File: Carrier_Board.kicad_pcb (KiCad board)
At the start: 4 copper layers, 190 x 110 mm, 269 parts, among them J10 Conn_01x03_Pin, J11 Conn_01x03_Pin, J12 Conn_01x04_Pin, J13 Conn_01x04_Pin, J14 Conn_01x03_Pin, J15 Bus_M.2_Socket_M, J16 Bus_M.2_Socket_E, J17 Barrel_Jack_Switch, J18 USB_C_Receptacle_USB2.0_16P, J19 Conn_01x04_Pin, J2 Bus_PCI_Express_x4, J20 Conn_01x04_Pin, J21 Conn_01x04_Pin, J3 HDMI_A, J4 USB3_A_Stacked, J5 USB_A_Stacked, J6 RJ45_RB1-125B8G1A, J7 Conn_01x04_Pin, J78 Conn_01x03_Pin, J8 Conn_01x03_Pin, J9 Conn_01x04_Pin, M1 Fan_4pin, M2 Fan_4pin, Q1 2N7002, Q2 2SK3018, Q3 2SK3018, Q5 2N7002, Q6 2N7002, Q7 AON7262E, Q8 2N7002, Q85 2SK3018, SW1 SW_Push, SW2 SW_Push, U1 D3V3XA4B10LP, U10 D3V3XA4B10LP, U11 D3V3XA4B10LP, U12 D3V3XA4B10LP, U13 TL431DBZ, U14 CH224K, U15 LM2734X, U16 LM2734X, U17 D3V3XA4B10LP, U2 D3V3XA4B10LP, U3 D3V3XA4B10LP, U4 D3V3XA4B10LP, U5 D3V3XA4B10LP, U6 RTL8111H-CG-RH, U7 D3V3XA4B10LP, U8 D3V3XA4B10LP, U9 D3V3XA4B10LP, Y1 25MHz

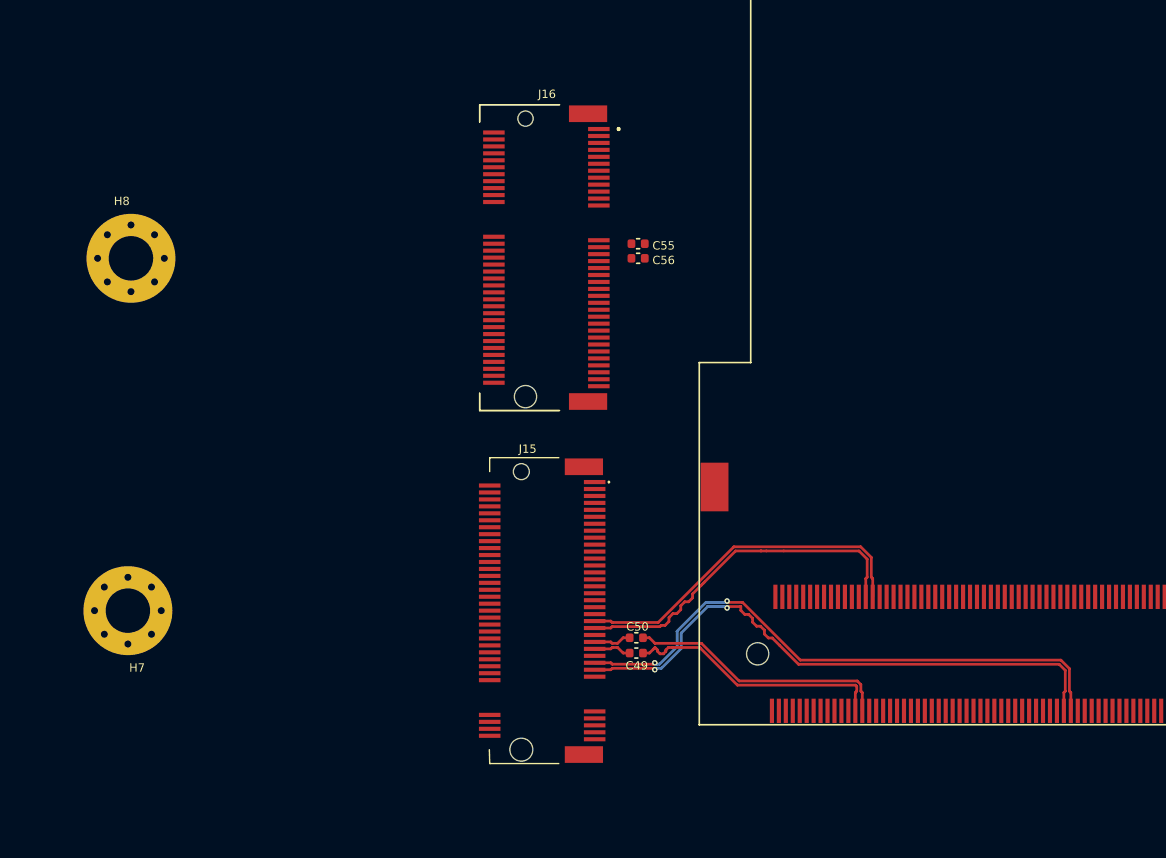
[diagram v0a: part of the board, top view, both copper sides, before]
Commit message: finished the differentail pair routing for the m.2 keys
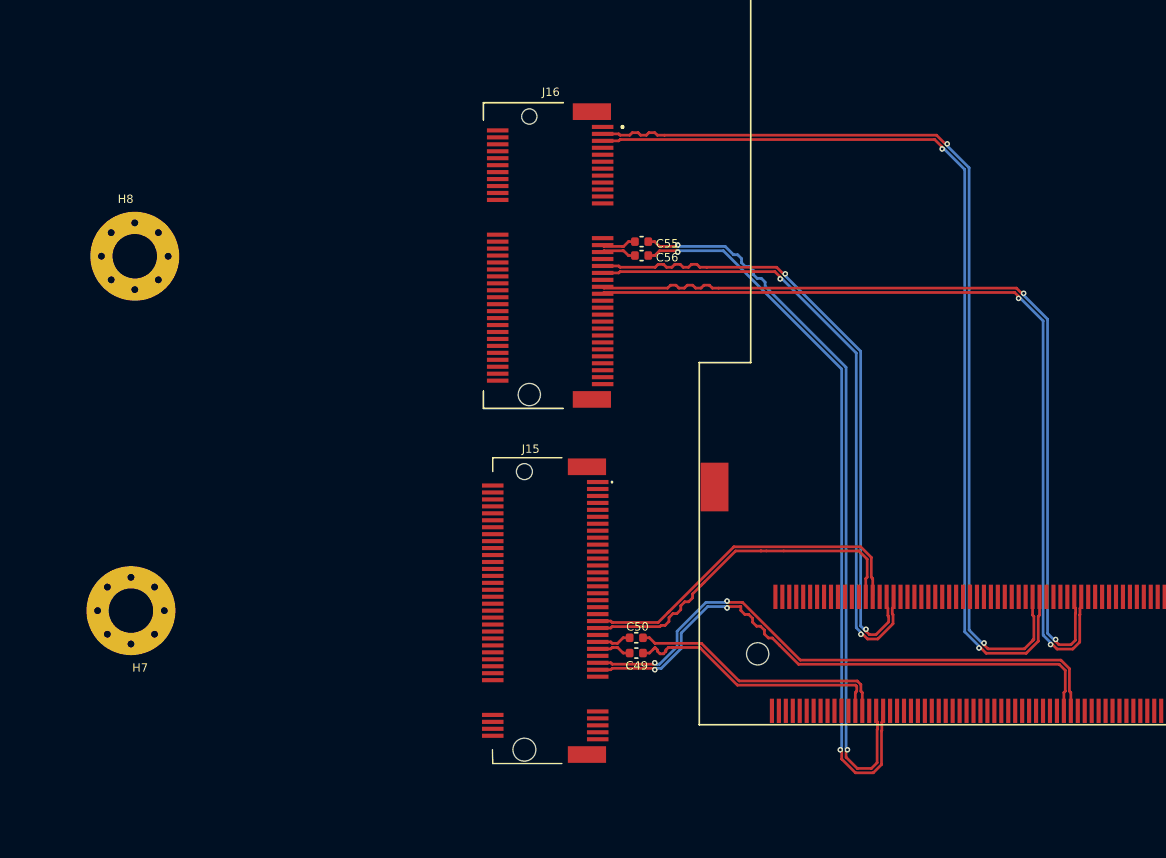
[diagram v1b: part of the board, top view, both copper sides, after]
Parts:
- moved C56 0.32 mm to (92.5, 82.0)
- moved H8 0.31 mm to (56.1, 82.0)
- moved J16 0.31 mm to (89.8, 72.7)
- moved C55 0.29 mm to (92.5, 81.0)
- moved H7 0.22 mm to (55.8, 107.5)
- moved J15 0.22 mm to (85.8, 107.5)
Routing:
- net /LattePanda Module/USB_2_P7+: track 0.00 -> 69.9 mm, vias 0 -> 2
- net /LattePanda Module/USB_2_P7-: track 0.00 -> 69.9 mm, vias 0 -> 2
- net /LattePanda Module/REFCLK3+: track 0.00 -> 61.9 mm, vias 0 -> 2
- net /LattePanda Module/REFCLK3-: track 0.00 -> 61.9 mm, vias 0 -> 2
- net /LattePanda Module/HSIO_3_TX+: track 0.00 -> 53.2 mm, vias 0 -> 2
- net /LattePanda Module/HSIO_3_TX-: track 0.00 -> 53.2 mm, vias 0 -> 2
- net /LattePanda Module/HSIO_3_RX+: track 0.00 -> 46.1 mm, vias 0 -> 2
- net /LattePanda Module/HSIO_3_RX-: track 0.00 -> 46.1 mm, vias 0 -> 2
- net /M.2 M Key/CON_PCIE_TX0+: track 0.00 -> 2.50 mm
- net /M.2 M Key/CON_PCIE_TX0-: track 0.00 -> 2.50 mm

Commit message: Created new Heiarchal sheet for audio, and started to arrange passive components for the HDMI connector
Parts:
- removed Q85: 2SK3018, A_HDJ_Library:SOT-23
- removed R143: 2.2K/1%, A_HDJ_Library:R_0402_1005Metric
- added Q4: 2SK3018, A_HDJ_Library:SOT-23, F.Cu at (152.3, 130.4)
- added R19: 2.2K/1%, A_HDJ_Library:R_0402_1005Metric, F.Cu at (149.4, 129.5)
- moved F2 321.5 mm to (86.6, 135.3)
- moved F3 321.5 mm to (86.6, 138.2)
- moved C30 308.3 mm to (86.6, 132.6)
- moved F4 305.1 mm to (103.3, 138.3)
- moved C31 293.1 mm to (103.3, 135.6)
- moved C26 287.2 mm to (107.6, 136.1)
- moved C27 287.2 mm to (107.6, 138.1)
- moved C32 285.1 mm to (111.2, 136.3)
- moved C28 284.1 mm to (107.8, 132.3)
- moved C29 284.1 mm to (107.8, 134.3)
- moved TP2 275.7 mm to (52.6, 122.1)
- moved Q1 272.2 mm to (131.0, 153.6)
- moved Q2 271.8 mm to (124.4, 142.7)
- moved Q3 271.8 mm to (124.4, 147.2)
- moved C17 259.9 mm to (131.8, 139.5)
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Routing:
- net Net-(J15-DEVSLP): track 0.00 -> 37.2 mm
- net Net-(D9-K): track 0.00 -> 13.9 mm
- net Net-(J16-SUSCLK): track 0.00 -> 3.63 mm
- net Net-(J16-~{W_DISABLE2}): track 0.00 -> 2.93 mm
- net Net-(J16-~{W_DISABLE1}): track 0.00 -> 2.64 mm
- net Net-(J15-SUSCLK): track 0.00 -> 2.53 mm
- net /M.2 M Key/CLKREQM: track 0.00 -> 2.53 mm
- net /M.2 M Key/CLKREQE: track 0.00 -> 2.29 mm
- net +3.3V: track 0.00 -> 1.20 mm

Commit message: HDM placement and some routing complete
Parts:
- moved C17 18.3 mm to (149.7, 136.0), turned to -90 degrees
- moved C18 17.8 mm to (148.7, 136.0), turned to -90 degrees
- moved C19 16.8 mm to (146.8, 135.9), turned to -90 degrees
- moved R19 15.7 mm to (160.2, 140.8)
- moved C20 11.7 mm to (145.8, 135.9), turned to -90 degrees
- moved C22 11.3 mm to (143.1, 135.9), turned to -90 degrees
- moved C21 10.9 mm to (144.1, 135.9), turned to -90 degrees
- moved Q4 10.6 mm to (157.2, 139.8), turned to 180 degrees
- moved U2 9.39 mm to (144.4, 143.5), turned to -90 degrees
- moved R7 9.13 mm to (139.5, 138.6)
- moved C24 6.02 mm to (140.0, 136.0), turned to -90 degrees
- moved C23 4.96 mm to (141.0, 136.0), turned to -90 degrees
- moved R10 3.89 mm to (144.3, 138.6)
- moved R9 3.76 mm to (142.7, 138.6)
- moved J6 3.60 mm to (164.4, 138.5)
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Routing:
- net /HDMI/DDI_B_TX3+: track 0.00 -> 26.6 mm
- net /HDMI/DDI_B_TX3-: track 0.00 -> 26.6 mm
- net /HDMI/DDI_B_TX2+: track 0.00 -> 26.0 mm
- net /HDMI/DDI_B_TX2-: track 0.00 -> 26.0 mm
- net /HDMI/DDI_B_TX1+: track 0.00 -> 25.5 mm
- net /HDMI/DDI_B_TX1-: track 0.00 -> 25.5 mm
- net /HDMI/DDI_B_TX0+: track 0.00 -> 25.0 mm
- net /HDMI/DDI_B_TX0-: track 0.00 -> 25.0 mm
- net /HDMI/TMDS_CK-: track 0.00 -> 14.3 mm
- net /HDMI/TMDS_CK+: track 0.00 -> 14.3 mm
- net /HDMI/TMDS_D0+: track 0.00 -> 12.7 mm
- net /HDMI/TMDS_D0-: track 0.00 -> 12.6 mm
- net /HDMI/TMDS_D2+: track 0.00 -> 12.3 mm
- net /HDMI/TMDS_D2-: track 0.00 -> 12.3 mm
- net /HDMI/TMDS_D1-: track 0.00 -> 12.1 mm
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
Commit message: HMI coponents placed and routed compete
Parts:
- removed R132, R134: 2.2k/1%, A_HDJ_Library:R_0402_1005Metric
- added R15: 2.2k/1%, A_HDJ_Library:R_0402_1005Metric, F.Cu at (135.5, 141.9)
- added R18: 2.2k/1%, A_HDJ_Library:R_0402_1005Metric, F.Cu at (133.9, 141.9)
- moved F1 274.5 mm to (131.8, 153.2)
- moved D4 273.3 mm to (131.3, 146.3), turned to -90 degrees
- moved C25 268.9 mm to (131.2, 151.8)
- moved D3 243.5 mm to (132.3, 141.9), turned to 90 degrees
- moved D1 240.5 mm to (137.1, 141.9), turned to 90 degrees
- moved C53 238.2 mm to (78.0, 97.3)
- moved C54 238.0 mm to (78.0, 98.3)
- moved C51 233.8 mm to (78.0, 95.3)
- moved C52 233.5 mm to (78.0, 96.3)
- moved C32 23.0 mm to (88.2, 136.3)
- moved C26 23.0 mm to (84.6, 136.1)
- moved C27 23.0 mm to (84.6, 138.1)
- moved C28 23.0 mm to (84.7, 132.3)
- moved C29 23.0 mm to (84.7, 134.3)
- moved C31 23.0 mm to (80.3, 135.6)
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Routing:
- net /HDMI/DDI_B_HPD: track 0.00 -> 38.8 mm, vias 0 -> 2
- net /HDMI/DDI_DDC_SCA: track 0.00 -> 28.6 mm
- net /HDMI/DDI_DDC_SCL: track 0.00 -> 28.2 mm
- net Net-(Q4-D): track 0.00 -> 19.8 mm, vias 0 -> 9
- net /HDMI/DDC_SCA: track 0.00 -> 16.5 mm
- net 5V_HDMI_VCC: track 0.00 -> 16.0 mm, vias 0 -> 2
- net /HDMI/HPD: track 0.00 -> 14.8 mm
- net /HDMI/DDC_SCL: track 0.00 -> 13.8 mm
- net Net-(J3-+5V): track 0.00 -> 12.4 mm
- net Net-(Q1-S): track 0.00 -> 4.52 mm
- net Net-(Q4-G): track 0.00 -> 2.07 mm

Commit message: positioning components for ehternet and USB connections and routing
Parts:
- moved U6 264.7 mm to (98.5, 128.2)
- moved U7 260.7 mm to (89.7, 128.5)
- moved U8 260.7 mm to (92.7, 128.5)
- moved BT78 169.2 mm to (220.7, 129.3)
- moved J10 168.9 mm to (205.1, 53.0)
- moved J11 168.9 mm to (191.7, 53.0)
- moved J14 168.9 mm to (196.4, 53.1)
- moved J8 168.9 mm to (200.8, 53.1)
- moved C46 77.9 mm to (94.3, 132.8)
- moved R24 77.9 mm to (90.0, 132.3)
- moved R25 77.9 mm to (90.0, 134.3)
- moved J6 77.9 mm to (86.5, 138.6)
- moved C26 15.8 mm to (68.9, 136.1)
- moved C27 15.8 mm to (68.9, 138.1)
- moved C28 15.8 mm to (69.0, 132.3)
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
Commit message: A little more adjusting before routing
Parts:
- moved U3 332.2 mm to (50.1, 144.3)
- moved F5 287.1 mm to (120.7, 135.9)
- moved U5 283.6 mm to (106.0, 137.8)
- moved U14 160.7 mm to (214.8, 83.2)
- moved Q7 149.2 mm to (198.3, 103.6)
- moved C31 54.1 mm to (118.5, 132.6)
- moved C28 48.9 mm to (117.8, 136.1)
- moved C29 48.9 mm to (117.8, 138.0)
- moved C26 6.25 mm to (63.9, 132.2)
- moved C27 6.25 mm to (63.9, 134.2)
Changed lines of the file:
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@@
 	(footprint "A_HDJ_Library:C_0603_1608Metric"
 		(layer "F.Cu")
-		(at 64.529999 135.59)
+		(at 118.5 132.55)
 		(descr "Capacitor SMD 0603 (1608 Metric), square (rectangular) end terminal, IPC_7351 nominal, (Body size source: IPC-SM-782 page 76, https://www.pcb-3d.com/wordpress/wp-content/uploads/ipc-sm-782a_amendment_1_and_2.pdf), generated with kicad-footprint-generator")
 		(tags "capacitor")
@@
 	(footprint "A_HDJ_Library:C_0402_1005Metric"
 		(layer "F.Cu")
-		(at 68.859999 136.09)
+		(at 63.93 132.25)
 		(descr "Capacitor SMD 0402 (1005 Metric), square (rectangular) end terminal, IPC_7351 nominal, (Body size source: IPC-SM-782 page 76, https://www.pcb-3d.com/wordpress/wp-content/uploads/ipc-sm-782a_amendment_1_and_2.pdf), generated with kicad-footprint-generator")
 		(tags "capacitor")
@@
 	(footprint "A_HDJ_Library:Fuse_0805_2012Metric"
 		(layer "F.Cu")
-		(at 379.325 11.15)
+		(at 120.7375 135.9)
 		(descr "Fuse SMD 0805 (2012 Metric), square (rectangular) end terminal, IPC_7351 nominal, (Body size source: https://docs.google.com/spreadsheets/d/1BsfQQcO9C6DZCsRaXUlFlo91Tg2WpOkGARC1WS5S8t0/edit?usp=sharing), generated with kicad-footprint-generator")
 		(tags "fuse")
@@
 	(footprint "A_HDJ_Library:MOSFET_PDFN8_3.3x3.3"
 		(layer "F.Cu")
-		(at 296.425 -8.825)
+		(at 198.3 103.56)
 		(descr " DFN 3x3  EP")
 		(tags "MOSFET (N-Channel)")
@@
 	(footprint "A_HDJ_Library:C_0402_1005Metric"
 		(layer "F.Cu")
-		(at 68.979999 132.34)
+		(at 117.775 136.05)
 		(descr "Capacitor SMD 0402 (1005 Metric), square (rectangular) end terminal, IPC_7351 nominal, (Body size source: IPC-SM-782 page 76, https://www.pcb-3d.com/wordpress/wp-content/uploads/ipc-sm-782a_amendment_1_and_2.pdf), generated with kicad-footprint-generator")
 		(tags "capacitor")
@@
 	(footprint "A_HDJ_Library:Diodes_UDFN-10_1.0x2.5mm_P0.5mm"
 		(layer "F.Cu")
-		(at 364.715 21.54)
+		(at 106.0375 137.8)
 		(descr "U-DFN2510-10 package used by Diodes Incorporated (https://www.diodes.com/assets/Package-Files/U-DFN2510-10-Type-CJ.pdf)")
 		(tags "UDFN-10 U-DFN2510-10 Diodes")
@@
 	(footprint "A_HDJ_Library:C_0402_1005Metric"
 		(layer "F.Cu")
-		(at 68.859999 138.06)
+		(at 63.93 134.22)
 		(descr "Capacitor SMD 0402 (1005 Metric), square (rectangular) end terminal, IPC_7351 nominal, (Body size source: IPC-SM-782 page 76, https://www.pcb-3d.com/wordpress/wp-content/uploads/ipc-sm-782a_amendment_1_and_2.pdf), generated with kicad-footprint-generator")
 		(tags "capacitor")
@@
 	(footprint "A_HDJ_Library:ESSOP-10-1EP_3.9x5mm_P1.0mm_EP3.2x2.3"
 		(layer "F.Cu")
-		(at 375.085 72.435227)
+		(at 214.75 83.15)
 		(property "Reference" "U14"
 			(at 3.71 1.78 270)
@@
 	(footprint "A_HDJ_Library:Diodes_UDFN-10_1.0x2.5mm_P0.5mm"
 		(layer "F.Cu")
-		(at 358.815 21.54)
+		(at 50.1 144.35)
 		(descr "U-DFN2510-10 package used by Diodes Incorporated (https://www.diodes.com/assets/Package-Files/U-DFN2510-10-Type-CJ.pdf)")
 		(tags "UDFN-10 U-DFN2510-10 Diodes")
@@
 	(footprint "A_HDJ_Library:C_0402_1005Metric"
 		(layer "F.Cu")
-		(at 68.979999 134.31)
+		(at 117.775 138.02)
 		(descr "Capacitor SMD 0402 (1005 Metric), square (rectangular) end terminal, IPC_7351 nominal, (Body size source: IPC-SM-782 page 76, https://www.pcb-3d.com/wordpress/wp-content/uploads/ipc-sm-782a_amendment_1_and_2.pdf), generated with kicad-footprint-generator")
 		(tags "capacitor")
